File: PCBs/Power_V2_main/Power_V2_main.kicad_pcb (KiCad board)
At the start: 2 copper layers, 100 x 100 mm, 49 parts, among them IC2 ADS1115BQDGSRQ1, IC3 ADS1115BQDGSRQ1, J10 TYPE-C-31-M-12, J11 Conn_01x04, J12 Conn_01x02, J13 Conn_01x04, J18 YK4420203000G, J2 Conn_01x02, J3 Conn_01x02, J4 PCIE-164-02-F-D-TH-TR, J5 PCIE-164-02-F-D-TH-TR, J6 PCIE-164-02-F-D-TH-TR, J7 TYPE-C-31-M-12, J8 PCIE-164-02-F-D-TH-TR, J9 Conn_01x02, U1 ESP32-S3-WROOM-2, U4 178.6164.0001, U5 TVS3300DRV, U6 USBLC6-4SC6, U9 AMS1117-3.3

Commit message: added LED indicators to board and redid power distribution in PCIe
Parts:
- added G***: LOGO, main_lib:IPRL_31mm, F.Cu at (241.0, 173.0)
- added J1: Conn_01x04, Connector_JST:JST_GH_BM04B-GHS-TBT_1x04-1MP_P1.25mm_Vertical, F.Cu at (204.6, 177.4)
- added Q2: RQ6E080AJ, Package_TO_SOT_SMD:TSOT-23-6, F.Cu at (219.0, 167.5)
- added Q3: RQ6E080AJ, Package_TO_SOT_SMD:TSOT-23-6, F.Cu at (213.5, 167.5)
- added R12: 500, Resistor_SMD:R_0805_2012Metric, F.Cu at (254.5, 142.5)
- added R13: 500, Resistor_SMD:R_0805_2012Metric, F.Cu at (256.5, 142.5)
- added R14: 500, Resistor_SMD:R_0805_2012Metric, F.Cu at (258.5, 142.5)
- added R15: 500, Resistor_SMD:R_0805_2012Metric, F.Cu at (260.5, 142.5)
- added R16: 500, Resistor_SMD:R_0805_2012Metric, F.Cu at (262.5, 142.5)
- added R4: 500, Resistor_SMD:R_0805_2012Metric, F.Cu at (250.5, 142.5)
- added R6: 500, Resistor_SMD:R_0805_2012Metric, F.Cu at (252.5, 142.5)
- R11: value 63 -> 500
- moved J9 7.46 mm to (226.5, 161.0)
- moved J18 1.95 mm to (281.8, 154.8)
- moved D1 1.51 mm to (250.0, 145.5)
- moved D4 1.50 mm to (250.0, 151.5)
- moved U5 1.50 mm to (255.1, 146.0)
- moved R11 1.33 mm to (248.5, 142.5), turned to 90 degrees
- moved U4 1.20 mm to (265.6, 149.7)
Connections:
- J4 pad A14: /14V8_PROTECTED -> GND
- J4 pad A15: /14V8_PROTECTED -> GND
- J4 pad A18: /14V8_PROTECTED -> GND
- J4 pad A19: /14V8_PROTECTED -> GND
- J4 pad A22: /14V8_PROTECTED -> GND
- J4 pad A23: /14V8_PROTECTED -> GND
- J4 pad A26: /14V8_PROTECTED -> GND
- J4 pad A27: /14V8_PROTECTED -> GND
- J4 pad A30: /14V8_PROTECTED -> GND
- J4 pad A31: /14V8_PROTECTED -> GND
- J4 pad A34: /14V8_PROTECTED -> GND
- J4 pad A35: /14V8_PROTECTED -> GND
- J4 pad A38: /14V8_PROTECTED -> GND
- J4 pad A39: /14V8_PROTECTED -> GND
- J4 pad A42: /14V8_PROTECTED -> GND
- J4 pad A43: /14V8_PROTECTED -> GND
- J4 pad A46: /14V8_PROTECTED -> GND
- J4 pad A47: /14V8_PROTECTED -> GND
- J4 pad A50: /14V8_PROTECTED -> GND
- J4 pad A51: /14V8_PROTECTED -> GND
- J4 pad A54: /14V8_PROTECTED -> GND
- J4 pad A55: /14V8_PROTECTED -> GND
- J4 pad A58: /14V8_PROTECTED -> GND
- J4 pad A59: /14V8_PROTECTED -> GND
- J4 pad A62: /14V8_PROTECTED -> GND
- J4 pad A63: /14V8_PROTECTED -> GND
- J4 pad A66: /14V8_PROTECTED -> GND
- J4 pad A67: /14V8_PROTECTED -> GND
- J4 pad A70: /14V8_PROTECTED -> GND
- J4 pad A71: /14V8_PROTECTED -> GND
- J4 pad A74: /14V8_PROTECTED -> GND
- J4 pad A75: /14V8_PROTECTED -> GND
- J4 pad A78: /14V8_PROTECTED -> GND
- J4 pad A79: /14V8_PROTECTED -> GND
- J4 pad A82: /14V8_PROTECTED -> GND
- J4 pad B12: GND -> /14V8_PROTECTED
- J4 pad B15: GND -> /14V8_PROTECTED
- J4 pad B16: GND -> /14V8_PROTECTED
- J4 pad B19: GND -> /14V8_PROTECTED
- J4 pad B20: GND -> /14V8_PROTECTED
- J4 pad B23: GND -> /14V8_PROTECTED
- J4 pad B24: GND -> /14V8_PROTECTED
- J4 pad B27: GND -> /14V8_PROTECTED
- J4 pad B28: GND -> /14V8_PROTECTED
- J4 pad B31: GND -> /14V8_PROTECTED
- J4 pad B32: GND -> /14V8_PROTECTED
- J4 pad B35: GND -> /14V8_PROTECTED
- J4 pad B36: GND -> /14V8_PROTECTED
- J4 pad B39: GND -> /14V8_PROTECTED
- J4 pad B40: GND -> /14V8_PROTECTED
- J4 pad B43: GND -> /14V8_PROTECTED
- J4 pad B44: GND -> /14V8_PROTECTED
- J4 pad B47: GND -> /14V8_PROTECTED
- J4 pad B48: GND -> /14V8_PROTECTED
- J4 pad B51: GND -> /14V8_PROTECTED
- J4 pad B52: GND -> /14V8_PROTECTED
- J4 pad B55: GND -> /14V8_PROTECTED
- J4 pad B56: GND -> /14V8_PROTECTED
- J4 pad B59: GND -> /14V8_PROTECTED
- J4 pad B60: GND -> /14V8_PROTECTED
- J4 pad B63: GND -> /14V8_PROTECTED
- J4 pad B64: GND -> /14V8_PROTECTED
- J4 pad B67: GND -> /14V8_PROTECTED
- J4 pad B68: GND -> /14V8_PROTECTED
- J4 pad B71: GND -> /14V8_PROTECTED
- J4 pad B72: GND -> /14V8_PROTECTED
- J4 pad B75: GND -> /14V8_PROTECTED
- J4 pad B76: GND -> /14V8_PROTECTED
- J4 pad B79: GND -> /14V8_PROTECTED
- J4 pad B80: GND -> /14V8_PROTECTED
- J5 pad A14: /14V8_PROTECTED -> GND
- J5 pad A15: /14V8_PROTECTED -> GND
- J5 pad A18: /14V8_PROTECTED -> GND
- J5 pad A19: /14V8_PROTECTED -> GND
- J5 pad A22: /14V8_PROTECTED -> GND
- J5 pad A23: /14V8_PROTECTED -> GND
- J5 pad A26: /14V8_PROTECTED -> GND
- J5 pad A27: /14V8_PROTECTED -> GND
- J5 pad A30: /14V8_PROTECTED -> GND
- J5 pad A31: /14V8_PROTECTED -> GND
- J5 pad A34: /14V8_PROTECTED -> GND
- J5 pad A35: /14V8_PROTECTED -> GND
- J5 pad A38: /14V8_PROTECTED -> GND
- J5 pad A39: /14V8_PROTECTED -> GND
- J5 pad A42: /14V8_PROTECTED -> GND
- J5 pad A43: /14V8_PROTECTED -> GND
- J5 pad A46: /14V8_PROTECTED -> GND
- J5 pad A47: /14V8_PROTECTED -> GND
- J5 pad A50: /14V8_PROTECTED -> GND
- J5 pad A51: /14V8_PROTECTED -> GND
- J5 pad A54: /14V8_PROTECTED -> GND
- J5 pad A55: /14V8_PROTECTED -> GND
- J5 pad A58: /14V8_PROTECTED -> GND
- J5 pad A59: /14V8_PROTECTED -> GND
- J5 pad A62: /14V8_PROTECTED -> GND
- J5 pad A63: /14V8_PROTECTED -> GND
- J5 pad A66: /14V8_PROTECTED -> GND
- J5 pad A67: /14V8_PROTECTED -> GND
- J5 pad A70: /14V8_PROTECTED -> GND
- J5 pad A71: /14V8_PROTECTED -> GND
- J5 pad A74: /14V8_PROTECTED -> GND
- J5 pad A75: /14V8_PROTECTED -> GND
- J5 pad A78: /14V8_PROTECTED -> GND
- J5 pad A79: /14V8_PROTECTED -> GND
- J5 pad A82: /14V8_PROTECTED -> GND
- J5 pad B12: GND -> /14V8_PROTECTED
- J5 pad B15: GND -> /14V8_PROTECTED
- J5 pad B16: GND -> /14V8_PROTECTED
- J5 pad B19: GND -> /14V8_PROTECTED
- J5 pad B20: GND -> /14V8_PROTECTED
- J5 pad B23: GND -> /14V8_PROTECTED
- J5 pad B24: GND -> /14V8_PROTECTED
- J5 pad B27: GND -> /14V8_PROTECTED
- J5 pad B28: GND -> /14V8_PROTECTED
- J5 pad B31: GND -> /14V8_PROTECTED
- J5 pad B32: GND -> /14V8_PROTECTED
- J5 pad B35: GND -> /14V8_PROTECTED
- J5 pad B36: GND -> /14V8_PROTECTED
- J5 pad B39: GND -> /14V8_PROTECTED
- J5 pad B40: GND -> /14V8_PROTECTED
- J5 pad B43: GND -> /14V8_PROTECTED
- J5 pad B44: GND -> /14V8_PROTECTED
- J5 pad B47: GND -> /14V8_PROTECTED
- J5 pad B48: GND -> /14V8_PROTECTED
- J5 pad B51: GND -> /14V8_PROTECTED
- J5 pad B52: GND -> /14V8_PROTECTED
- J5 pad B55: GND -> /14V8_PROTECTED
- J5 pad B56: GND -> /14V8_PROTECTED
- J5 pad B59: GND -> /14V8_PROTECTED
- J5 pad B60: GND -> /14V8_PROTECTED
- J5 pad B63: GND -> /14V8_PROTECTED
- J5 pad B64: GND -> /14V8_PROTECTED
- J5 pad B67: GND -> /14V8_PROTECTED
- J5 pad B68: GND -> /14V8_PROTECTED
- J5 pad B71: GND -> /14V8_PROTECTED
- J5 pad B72: GND -> /14V8_PROTECTED
- J5 pad B75: GND -> /14V8_PROTECTED
- J5 pad B76: GND -> /14V8_PROTECTED
- J5 pad B79: GND -> /14V8_PROTECTED
- J5 pad B80: GND -> /14V8_PROTECTED
- J6 pad A14: /14V8_PROTECTED -> GND
- J6 pad A15: /14V8_PROTECTED -> GND
- J6 pad A18: /14V8_PROTECTED -> GND
- J6 pad A19: /14V8_PROTECTED -> GND
- J6 pad A22: /14V8_PROTECTED -> GND
- J6 pad A23: /14V8_PROTECTED -> GND
- J6 pad A26: /14V8_PROTECTED -> GND
- J6 pad A27: /14V8_PROTECTED -> GND
- J6 pad A30: /14V8_PROTECTED -> GND
- J6 pad A31: /14V8_PROTECTED -> GND
- J6 pad A34: /14V8_PROTECTED -> GND
- J6 pad A35: /14V8_PROTECTED -> GND
- J6 pad A38: /14V8_PROTECTED -> GND
- J6 pad A39: /14V8_PROTECTED -> GND
- J6 pad A42: /14V8_PROTECTED -> GND
- J6 pad A43: /14V8_PROTECTED -> GND
- J6 pad A46: /14V8_PROTECTED -> GND
- J6 pad A47: /14V8_PROTECTED -> GND
- J6 pad A50: /14V8_PROTECTED -> GND
- J6 pad A51: /14V8_PROTECTED -> GND
- J6 pad A54: /14V8_PROTECTED -> GND
- J6 pad A55: /14V8_PROTECTED -> GND
- J6 pad A58: /14V8_PROTECTED -> GND
- J6 pad A59: /14V8_PROTECTED -> GND
- J6 pad A62: /14V8_PROTECTED -> GND
- J6 pad A63: /14V8_PROTECTED -> GND
- J6 pad A66: /14V8_PROTECTED -> GND
- J6 pad A67: /14V8_PROTECTED -> GND
- J6 pad A70: /14V8_PROTECTED -> GND
- J6 pad A71: /14V8_PROTECTED -> GND
- J6 pad A74: /14V8_PROTECTED -> GND
- J6 pad A75: /14V8_PROTECTED -> GND
- J6 pad A78: /14V8_PROTECTED -> GND
- J6 pad A79: /14V8_PROTECTED -> GND
- J6 pad A82: /14V8_PROTECTED -> GND
- J6 pad B12: GND -> /14V8_PROTECTED
- J6 pad B15: GND -> /14V8_PROTECTED
- J6 pad B16: GND -> /14V8_PROTECTED
- J6 pad B19: GND -> /14V8_PROTECTED
- J6 pad B20: GND -> /14V8_PROTECTED
- J6 pad B23: GND -> /14V8_PROTECTED
- J6 pad B24: GND -> /14V8_PROTECTED
- J6 pad B27: GND -> /14V8_PROTECTED
- J6 pad B28: GND -> /14V8_PROTECTED
- J6 pad B31: GND -> /14V8_PROTECTED
- J6 pad B32: GND -> /14V8_PROTECTED
- J6 pad B35: GND -> /14V8_PROTECTED
- J6 pad B36: GND -> /14V8_PROTECTED
- J6 pad B39: GND -> /14V8_PROTECTED
- J6 pad B40: GND -> /14V8_PROTECTED
- J6 pad B43: GND -> /14V8_PROTECTED
- J6 pad B44: GND -> /14V8_PROTECTED
- J6 pad B47: GND -> /14V8_PROTECTED
- J6 pad B48: GND -> /14V8_PROTECTED
- J6 pad B51: GND -> /14V8_PROTECTED
- J6 pad B52: GND -> /14V8_PROTECTED
- J6 pad B55: GND -> /14V8_PROTECTED
- J6 pad B56: GND -> /14V8_PROTECTED
- J6 pad B59: GND -> /14V8_PROTECTED
- J6 pad B60: GND -> /14V8_PROTECTED
- J6 pad B63: GND -> /14V8_PROTECTED
- J6 pad B64: GND -> /14V8_PROTECTED
- J6 pad B67: GND -> /14V8_PROTECTED
- J6 pad B68: GND -> /14V8_PROTECTED
- J6 pad B71: GND -> /14V8_PROTECTED
- J6 pad B72: GND -> /14V8_PROTECTED
- J6 pad B75: GND -> /14V8_PROTECTED
- J6 pad B76: GND -> /14V8_PROTECTED
- J6 pad B79: GND -> /14V8_PROTECTED
- J6 pad B80: GND -> /14V8_PROTECTED
- J8 pad A14: /14V8_PROTECTED -> GND
- J8 pad A15: /14V8_PROTECTED -> GND
- J8 pad A18: /14V8_PROTECTED -> GND
- J8 pad A19: /14V8_PROTECTED -> GND
- J8 pad A22: /14V8_PROTECTED -> GND
- J8 pad A23: /14V8_PROTECTED -> GND
- J8 pad A26: /14V8_PROTECTED -> GND
- J8 pad A27: /14V8_PROTECTED -> GND
- J8 pad A30: /14V8_PROTECTED -> GND
- J8 pad A31: /14V8_PROTECTED -> GND
- J8 pad A34: /14V8_PROTECTED -> GND
- J8 pad A35: /14V8_PROTECTED -> GND
- J8 pad A38: /14V8_PROTECTED -> GND
- J8 pad A39: /14V8_PROTECTED -> GND
- J8 pad A42: /14V8_PROTECTED -> GND
- J8 pad A43: /14V8_PROTECTED -> GND
- J8 pad A46: /14V8_PROTECTED -> GND
- J8 pad A47: /14V8_PROTECTED -> GND
- J8 pad A50: /14V8_PROTECTED -> GND
- J8 pad A51: /14V8_PROTECTED -> GND
- J8 pad A54: /14V8_PROTECTED -> GND
- J8 pad A55: /14V8_PROTECTED -> GND
- J8 pad A58: /14V8_PROTECTED -> GND
- J8 pad A59: /14V8_PROTECTED -> GND
- J8 pad A62: /14V8_PROTECTED -> GND
- J8 pad A63: /14V8_PROTECTED -> GND
- J8 pad A66: /14V8_PROTECTED -> GND
- J8 pad A67: /14V8_PROTECTED -> GND
- J8 pad A70: /14V8_PROTECTED -> GND
- J8 pad A71: /14V8_PROTECTED -> GND
- J8 pad A74: /14V8_PROTECTED -> GND
- J8 pad A75: /14V8_PROTECTED -> GND
- J8 pad A78: /14V8_PROTECTED -> GND
- J8 pad A79: /14V8_PROTECTED -> GND
- J8 pad A82: /14V8_PROTECTED -> GND
- J8 pad B12: GND -> /14V8_PROTECTED
- J8 pad B15: GND -> /14V8_PROTECTED
- J8 pad B16: GND -> /14V8_PROTECTED
- J8 pad B19: GND -> /14V8_PROTECTED
- J8 pad B20: GND -> /14V8_PROTECTED
- J8 pad B23: GND -> /14V8_PROTECTED
- J8 pad B24: GND -> /14V8_PROTECTED
- J8 pad B27: GND -> /14V8_PROTECTED
- J8 pad B28: GND -> /14V8_PROTECTED
- J8 pad B31: GND -> /14V8_PROTECTED
- J8 pad B32: GND -> /14V8_PROTECTED
- J8 pad B35: GND -> /14V8_PROTECTED
- J8 pad B36: GND -> /14V8_PROTECTED
- J8 pad B39: GND -> /14V8_PROTECTED
- J8 pad B40: GND -> /14V8_PROTECTED
- J8 pad B43: GND -> /14V8_PROTECTED
- J8 pad B44: GND -> /14V8_PROTECTED
- J8 pad B47: GND -> /14V8_PROTECTED
- J8 pad B48: GND -> /14V8_PROTECTED
- J8 pad B51: GND -> /14V8_PROTECTED
- J8 pad B52: GND -> /14V8_PROTECTED
- J8 pad B55: GND -> /14V8_PROTECTED
- J8 pad B56: GND -> /14V8_PROTECTED
- J8 pad B59: GND -> /14V8_PROTECTED
- J8 pad B60: GND -> /14V8_PROTECTED
- J8 pad B63: GND -> /14V8_PROTECTED
- J8 pad B64: GND -> /14V8_PROTECTED
- J8 pad B67: GND -> /14V8_PROTECTED
- J8 pad B68: GND -> /14V8_PROTECTED
- J8 pad B71: GND -> /14V8_PROTECTED
- J8 pad B72: GND -> /14V8_PROTECTED
- J8 pad B75: GND -> /14V8_PROTECTED
- J8 pad B76: GND -> /14V8_PROTECTED
- J8 pad B79: GND -> /14V8_PROTECTED
- J8 pad B80: GND -> /14V8_PROTECTED
- U1 pad 15: unconnected-(U1-IO3-Pad15) -> /Control/IND_GREEN
- U1 pad 21: unconnected-(U1-IO13-Pad21) -> /Control/IND_YELLOW
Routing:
- net /LED Indicators/YELLOW_OUT: track 0.00 -> 21.3 mm
- net /LED Indicators/GREEN_OUT: track 0.00 -> 16.5 mm
- net /14V8_PROTECTED: track 6.09 -> 20.4 mm
- net /Protection and power/EMERG_OUT: track 16.1 -> 29.5 mm
- net GND: track 104.3 -> 117.1 mm, vias 11 -> 12
- net /Control/IND_YELLOW: track 0.00 -> 11.3 mm, vias 0 -> 2
- net /Control/IND_GREEN: track 0.00 -> 11.0 mm, vias 0 -> 2
- net Net-(J9-Pin_2): track 12.8 -> 5.38 mm
- net Net-(J12-Pin_2): track 18.0 -> 20.5 mm
- net /Connector Drive/OUT_READ: track 76.2 -> 78.6 mm
- net /Connector Comms/OUT_READ: track 121.5 -> 123.9 mm
- net /Connector Arm/OUT_READ: track 108.9 -> 111.3 mm
- net /Connector Drill/OUT_READ: track 98.1 -> 100.5 mm
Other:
- board text added: "ARM"
- board text added: "COMMS"
- board text added: "DRILL"
- board text added: "DRIVE"
- board text added: "Designed by James King"
- board text added: "ESTOP"
- board text added: "POWER BOARD: MAIN"
- board text added: "POWER DATA"
- board text added: "RELAY GND"

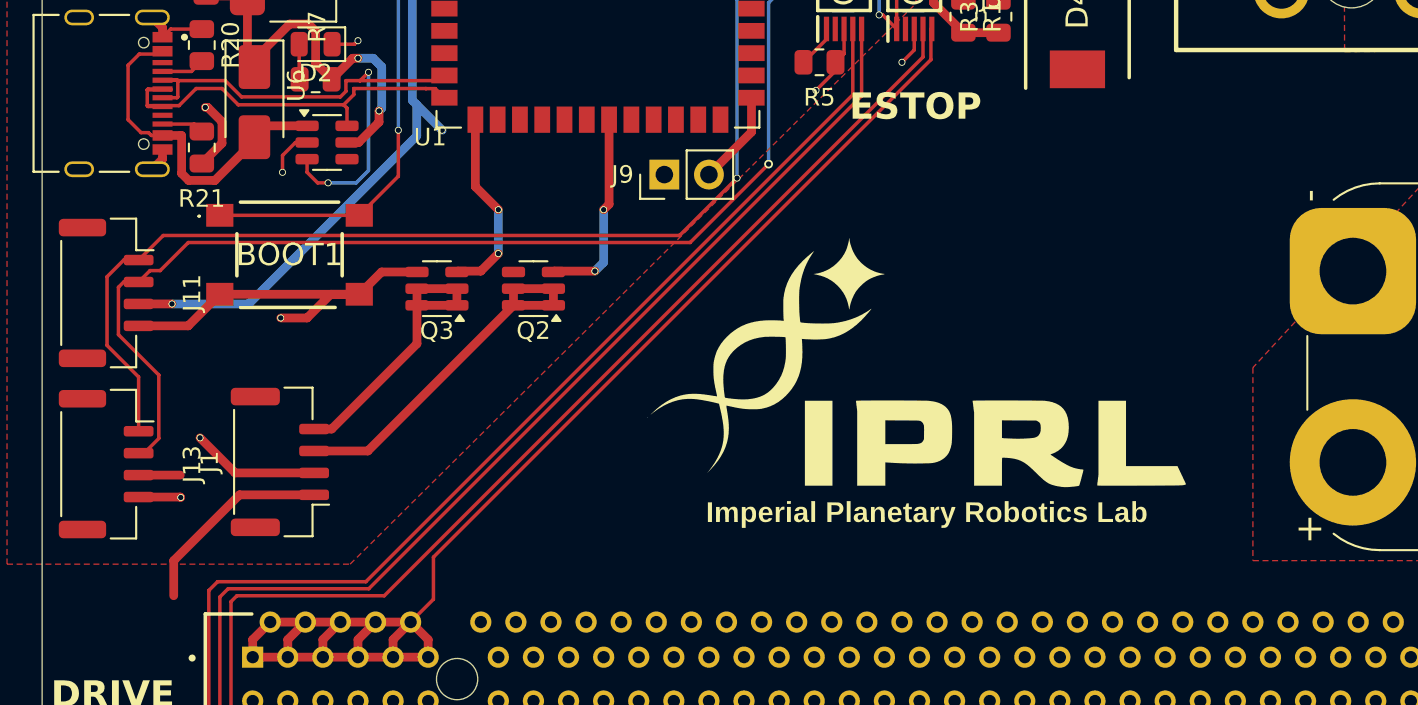
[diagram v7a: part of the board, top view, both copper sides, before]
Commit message: modification to LED switches
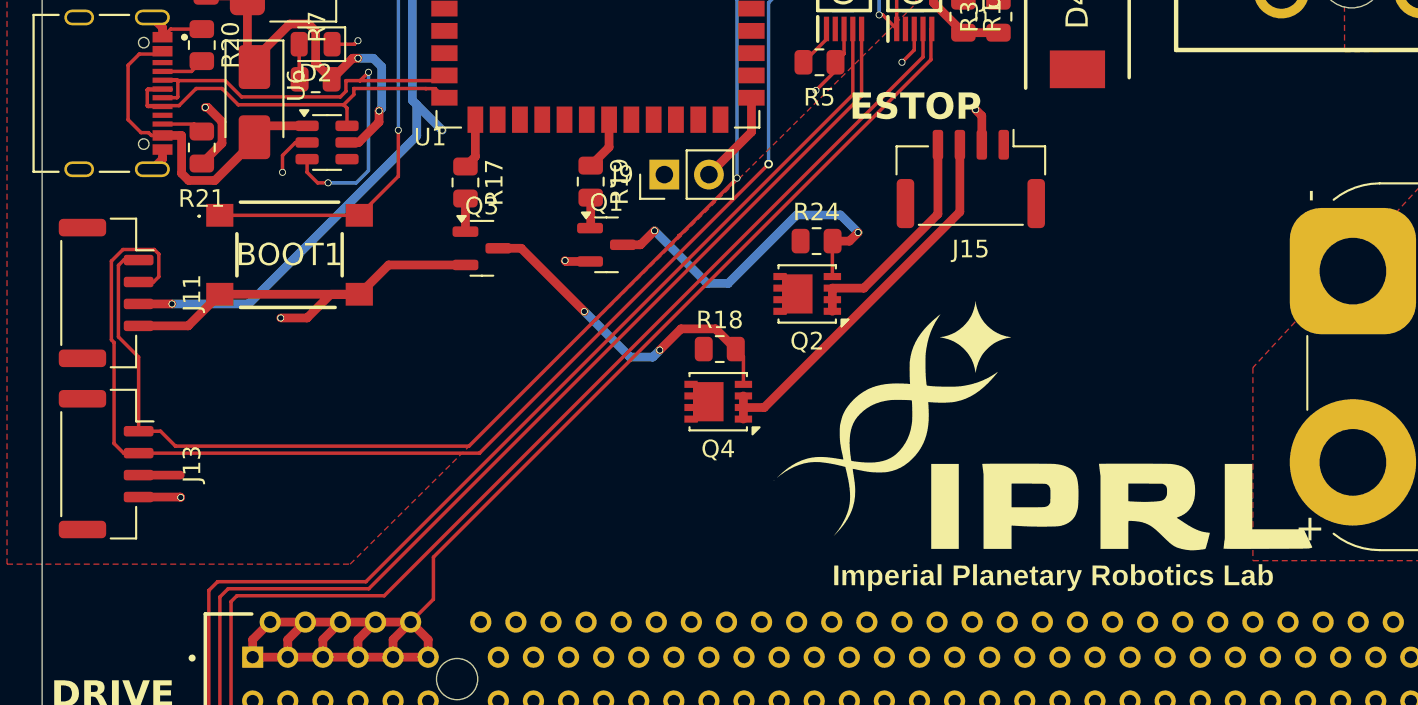
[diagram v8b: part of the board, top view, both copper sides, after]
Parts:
- removed J1: Conn_01x04, Connector_JST:JST_GH_BM04B-GHS-TBT_1x04-1MP_P1.25mm_Vertical
- added J15: Conn_01x04, Connector_JST:JST_GH_BM04B-GHS-TBT_1x04-1MP_P1.25mm_Vertical, F.Cu at (243.9, 161.2)
- added Q1: BC846, Package_TO_SOT_SMD:SOT-23, F.Cu at (223.2, 165.0)
- added Q4: SiSS27DN, Package_SO:Vishay_PowerPAK_1212-8_Single, F.Cu at (229.5, 173.9)
- added R17: 1k, Resistor_SMD:R_0805_2012Metric, F.Cu at (215.1, 161.4)
- added R18: 5k, Resistor_SMD:R_0805_2012Metric, F.Cu at (229.6, 170.9)
- added R19: 1k, Resistor_SMD:R_0805_2012Metric, F.Cu at (222.3, 161.4)
- added R24: 5k, Resistor_SMD:R_0805_2012Metric, F.Cu at (235.1, 164.8)
- Q2: value RQ6E080AJ -> SiSS27DN; footprint Package_TO_SOT_SMD:TSOT-23-6 -> Package_SO:Vishay_PowerPAK_1212-8_Single
- Q3: value RQ6E080AJ -> BC846; footprint Package_TO_SOT_SMD:TSOT-23-6 -> Package_TO_SOT_SMD:SOT-23
- moved Q2 15.6 mm to (234.6, 167.8)
- moved G*** 8.05 mm to (248.2, 176.6)
- moved Q3 3.44 mm to (216.1, 165.2), turned to 0 degrees
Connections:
- Q2 pad 1: /LED Indicators/YELLOW_OUT -> /LED Indicators/GREEN_OUT
- Q2 pad 2: /LED Indicators/YELLOW_OUT -> /LED Indicators/GREEN_OUT
- Q2 pad 3: /Control/IND_YELLOW -> /LED Indicators/GREEN_OUT
- Q2 pad 4: GND -> /LED Indicators/Green switch/GATE
- Q2 pad 5: /LED Indicators/YELLOW_OUT -> /14V8_PROTECTED
- Q3 pad 1: /LED Indicators/GREEN_OUT -> /LED Indicators/Yellow switch/BASE
- Q3 pad 2: /LED Indicators/GREEN_OUT -> GND
- Q3 pad 3: /Control/IND_GREEN -> /LED Indicators/Yellow switch/GATE
- U1 pad 15: /Control/IND_GREEN -> /Control/IND_YELLOW
- U1 pad 21: /Control/IND_YELLOW -> /Control/IND_GREEN
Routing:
- net /LED Indicators/Green switch/GATE: track 0.00 -> 20.7 mm, vias 0 -> 2
- net /LED Indicators/Yellow switch/GATE: track 0.00 -> 19.4 mm, vias 0 -> 2
- net /14V8_PROTECTED: track 20.4 -> 8.82 mm
- net /Control/SDA: track 80.5 -> 90.0 mm
- net /Control/IND_YELLOW: track 11.3 -> 2.90 mm, vias 2 -> 0
- net /Control/IND_GREEN: track 11.0 -> 3.05 mm, vias 2 -> 0
- net /Control/SCL: track 81.6 -> 85.8 mm
- net /LED Indicators/GREEN_OUT: track 16.5 -> 13.0 mm
- net /LED Indicators/Yellow switch/BASE: track 0.00 -> 1.89 mm
- net /LED Indicators/Green switch/BASE: track 0.00 -> 1.75 mm
- net /LED Indicators/YELLOW_OUT: track 21.3 -> 22.1 mm
- net GND: track 117.1 -> 116.2 mm, vias 12 -> 13
